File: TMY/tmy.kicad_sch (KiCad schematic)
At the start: 54 parts, among them J1 H1+, J2 H-, J3 LCD, Q1 12P10V, Q2 DTC143E, Q3 DTC143E, Q4 CJE3139K, Q5 LMUN2232LT1G, U1 CS32F031K8V6, U2 ZB 25VQ32, U3 TP4054, U4 LDO

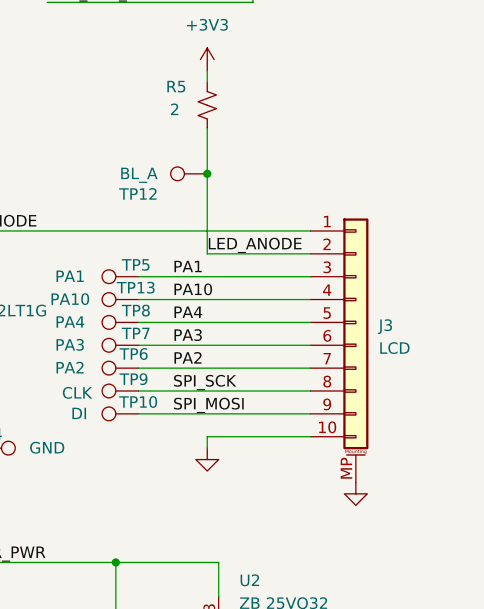
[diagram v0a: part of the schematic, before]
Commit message: add LCD pinout
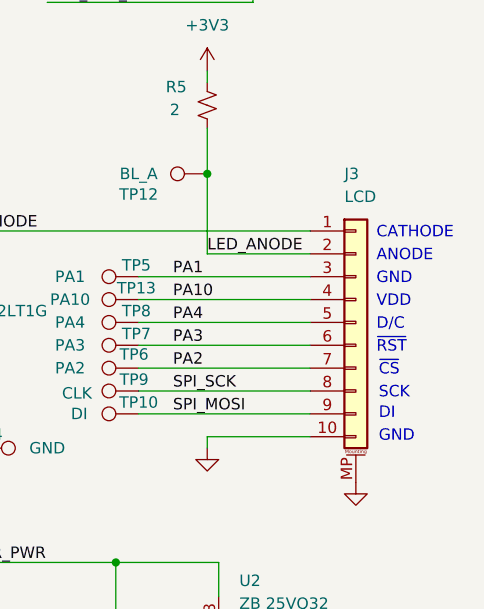
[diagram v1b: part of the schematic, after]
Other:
- note added: "ANODE"
- note added: "CATHODE"
- note added: "D/C"
- note added: "DI"
- note added: "GND"
- note added: "SCK"
- note added: "VDD"
- note added: "~{CS}"
- note added: "~{RST}"
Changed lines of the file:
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@@
 		)
 	)
+	(text "~{CS}"
+		(exclude_from_sim no)
+		(at 270.51 106.934 0)
+		(effects
+			(font
+				(size 1.27 1.27)
+			)
+			(justify left)
+		)
+	)
+	(text "DI"
+		(exclude_from_sim no)
+		(at 270.51 111.76 0)
+		(effects
+			(font
+				(size 1.27 1.27)
+			)
+			(justify left)
+		)
+	)
+	(text "~{RST}"
+		(exclude_from_sim no)
+		(at 270.256 104.394 0)
+		(effects
+			(font
+				(size 1.27 1.27)
+			)
+			(justify left)
+		)
+	)
 	(text "TIM1_CH4"
 		(exclude_from_sim no)
@@
 		)
 	)
+	(text "SCK"
+		(exclude_from_sim no)
+		(at 270.51 109.474 0)
+		(effects
+			(font
+				(size 1.27 1.27)
+			)
+			(justify left)
+		)
+	)
 	(text "SWCLK"
 		(exclude_from_sim no)
@@
 		)
 	)
+	(text "GND"
+		(exclude_from_sim no)
+		(at 270.51 114.3 0)
+		(effects
+			(font
+				(size 1.27 1.27)
+			)
+			(justify left)
+		)
+	)
+	(text "GND"
+		(exclude_from_sim no)
+		(at 270.256 96.774 0)
+		(effects
+			(font
+				(size 1.27 1.27)
+			)
+			(justify left)
+		)
+	)
 	(text "TIM1_CH1"
 		(exclude_from_sim no)
@@
 		)
 	)
+	(text "ANODE"
+		(exclude_from_sim no)
+		(at 270.256 94.234 0)
+		(effects
+			(font
+				(size 1.27 1.27)
+			)
+			(justify left)
+		)
+	)
 	(text "SPI1_MOSI"
 		(exclude_from_sim no)
@@
 		)
 	)
+	(text "CATHODE"
+		(exclude_from_sim no)
+		(at 270.256 91.694 0)
+		(effects
+			(font
+				(size 1.27 1.27)
+			)
+			(justify left)
+		)
+	)
+	(text "D/C"
+		(exclude_from_sim no)
+		(at 270.256 101.854 0)
+		(effects
+			(font
+				(size 1.27 1.27)
+			)
+			(justify left)
+		)
+	)
+	(text "VDD"
+		(exclude_from_sim no)
+		(at 270.256 99.314 0)
+		(effects
+			(font
+				(size 1.27 1.27)
+			)
+			(justify left)
+		)
+	)
 	(junction
 		(at 91.44 57.15)
@@
 		(on_board yes)
 		(dnp no)
-		(fields_autoplaced yes)
 		(property "Reference" "J3"
-			(at 270.51 101.9555 0)
+			(at 266.7 85.09 0)
 			(effects
 				(font
@@
 		)
 		(property "Value" "LCD"
-			(at 270.51 104.4955 0)
+			(at 266.7 87.63 0)
 			(effects
 				(font
